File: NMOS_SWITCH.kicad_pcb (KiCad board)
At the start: 2 copper layers, 35 x 25 mm, 23 parts, among them J1 Conn_01x02, J2 Conn_01x02, J3 Conn_01x02, Q1 Q_NPN_BCE, Q2 CSD18540Q5B, U1 BTS443P, U2 LM5050-1

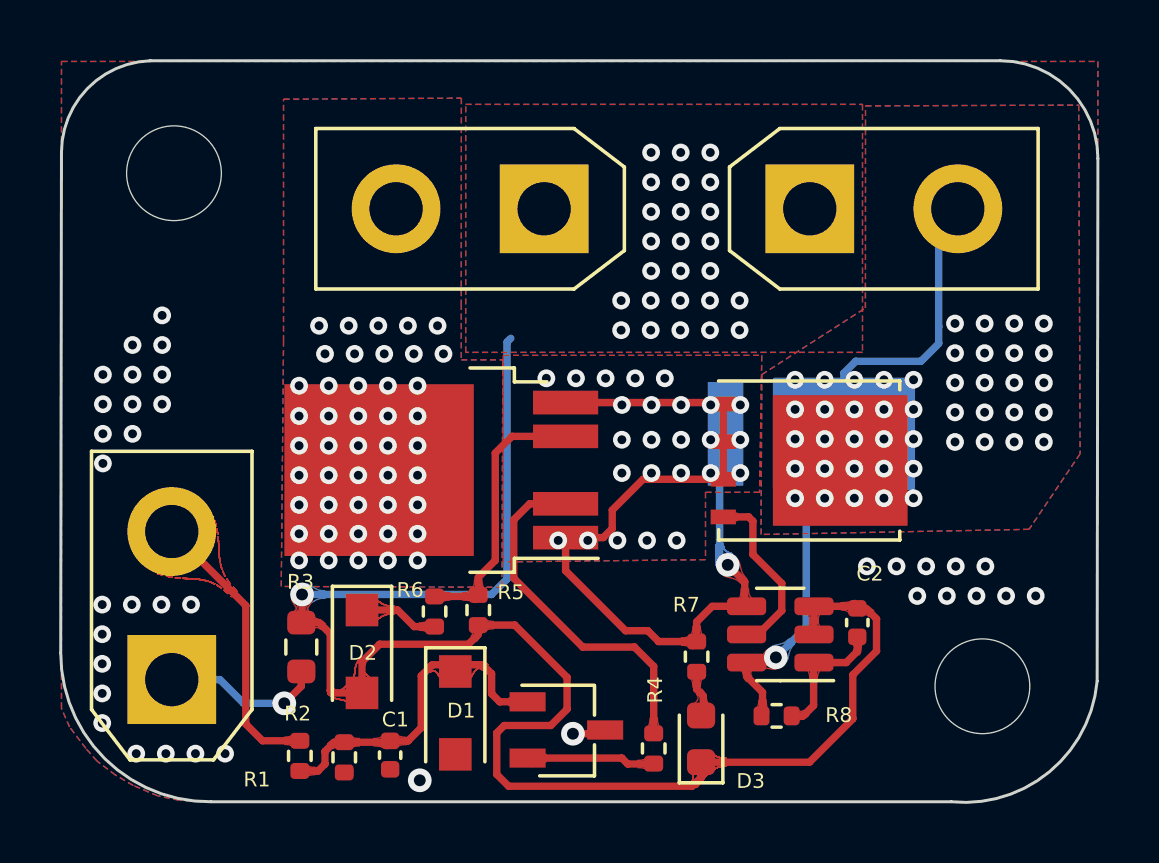
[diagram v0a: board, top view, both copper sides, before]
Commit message: Change some footprints
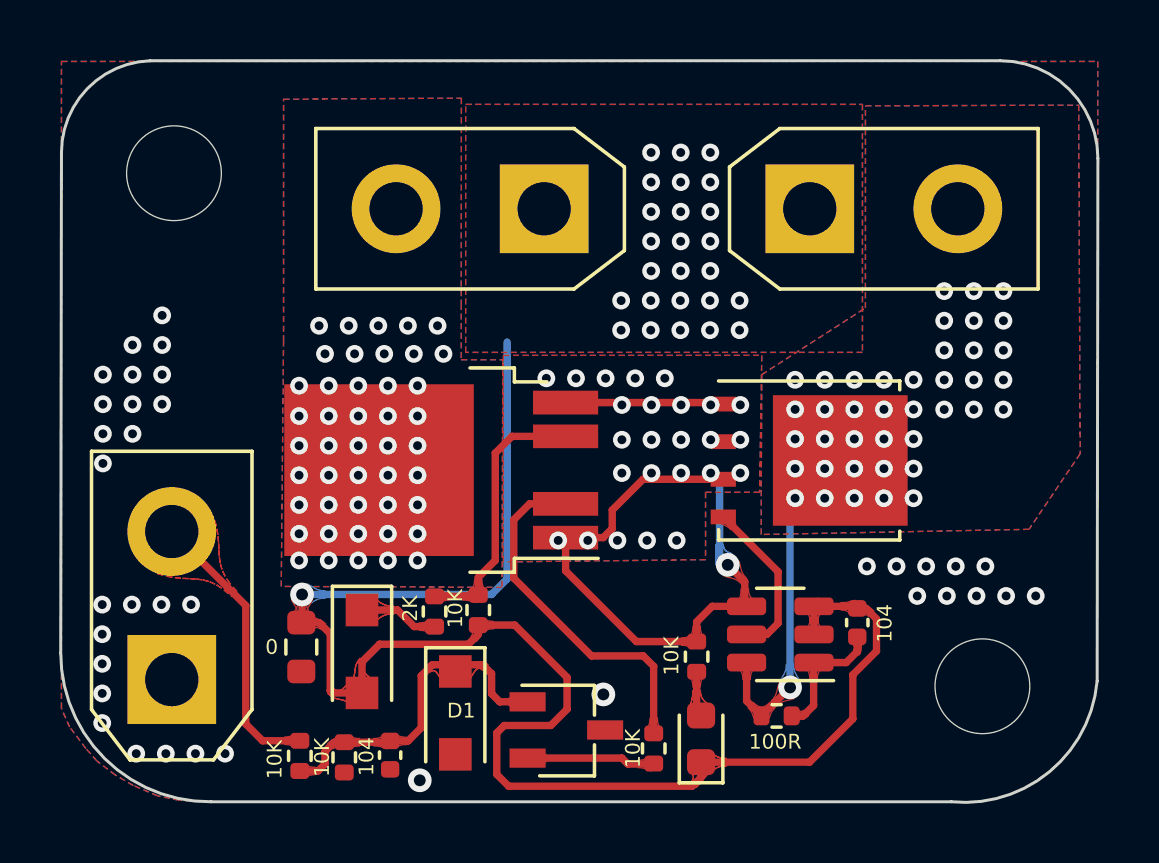
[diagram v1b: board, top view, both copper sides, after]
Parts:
- removed D4: SVM1550UB, POWER_DIODE_SMD:TO-277A
- renumbered R3 to 0, R8 to 100R, C1 to 104, C2 to 104, R4 to 10K, R1 to 10K, R5 to 10K, R7 to 10K, R2 to 10K, R6 to 2K
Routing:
- net /NMOS_OUT: track 22.7 -> 8.84 mm, vias 46 -> 41
- net GND: track 6.59 -> 0.00 mm, vias 37 -> 36
- net Net-(Q2-Pad1): track 28.0 -> 25.4 mm
